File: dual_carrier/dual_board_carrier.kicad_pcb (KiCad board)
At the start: 2 copper layers, 63 x 36.6 mm, 28 parts, among them J1 Conn_01x08, J2 Conn_01x08, J3 Conn_02x10_Top_Bottom, J4 Conn_01x08, J5 Conn_01x08, U1 TJA1051T-3, U2 LM78M05_TO252, U3 TJA1051T-3

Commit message: Add files via upload
Dual Carrier v0.2
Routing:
- net GND: track 79.2 -> 70.7 mm, vias 24 -> 20
- net /CAN_H: track 66.8 -> 62.7 mm
- net +5V: track 101.0 -> 100.4 mm
- added copper zone on F.Cu, net GND
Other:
- board text added: "Dual wideband LSU 4.9 Controller - rusEFI https://rusefi.com/forum/viewtopic.php?f=4&t=1856 https://rusefi.com/forum/viewtopic.php?f=4&t=1927"

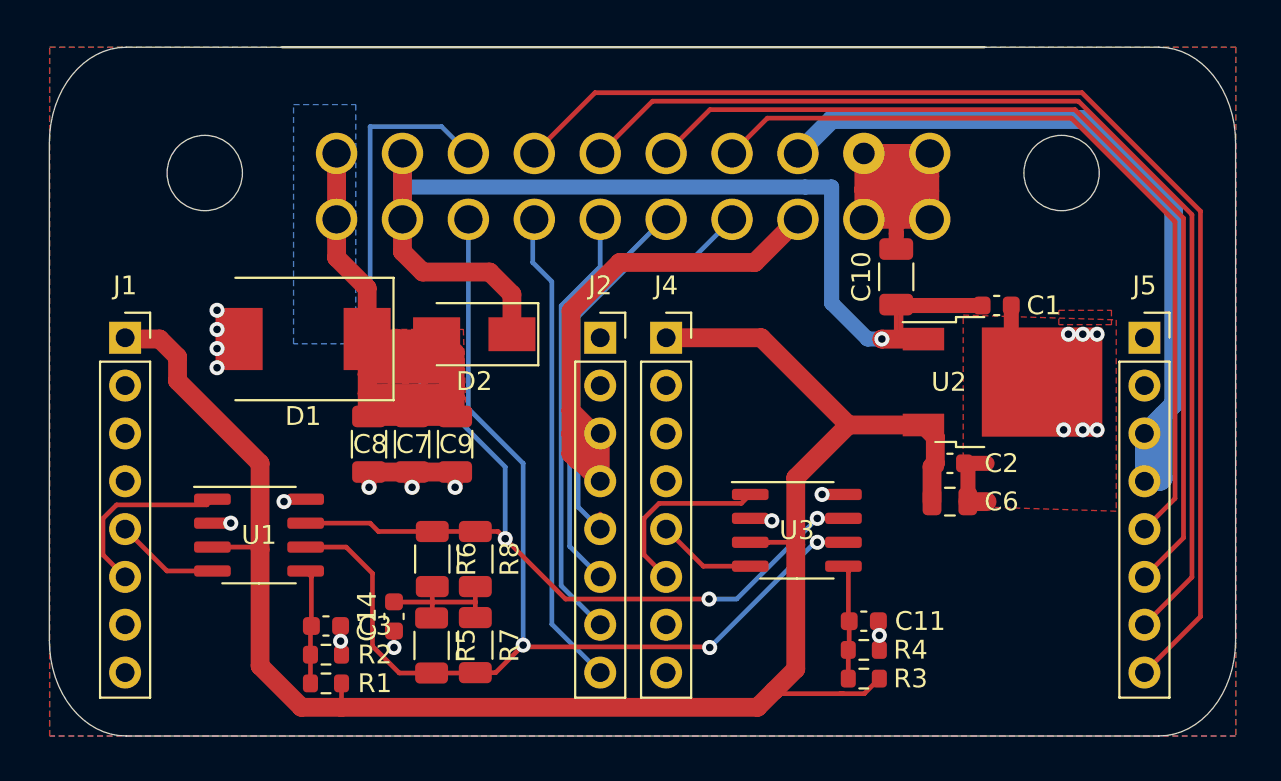
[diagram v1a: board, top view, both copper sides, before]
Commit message: Add files via upload
02/07/21 Updates to dual_carrier and creation of dual_carrier_sxs
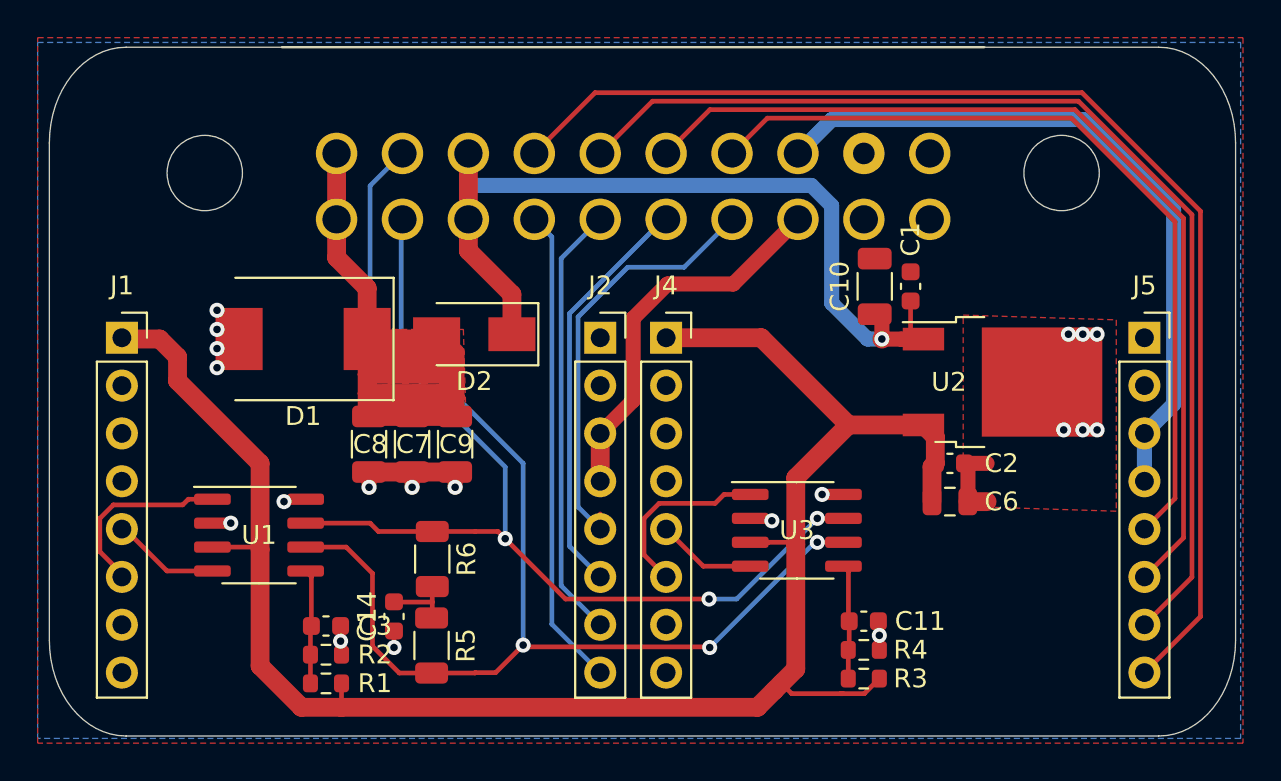
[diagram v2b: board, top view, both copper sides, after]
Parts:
- removed R7, R8: 120, Resistor_SMD:R_1206_3216Metric
- R5, R6: value 120 -> 60
- moved C1 4.68 mm to (144.3, 80.8), turned to 90 degrees
- moved C10 1.25 mm to (142.4, 80.8)
- moved J1 0.17 mm to (102.4, 83.5)
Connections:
- J3 pad 18: /CAN_H -> /LSU_Heater+
- J3 pad 19: /LSU_Heater+ -> /CAN_H
- J3 pad 8: /CAN_L -> /LSU_Heater+
- J3 pad 9: /LSU_Heater+ -> /CAN_L
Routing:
- net GND: track 70.7 -> 26.6 mm
- net /LSU_Heater+: track 63.7 -> 50.2 mm
- net /LSU1_Heater-: track 33.2 -> 20.9 mm
- net /CAN_H: track 62.7 -> 56.1 mm
- net /LSU2_Heater-: track 42.2 -> 37.7 mm
- net Net-(C14-Pad2): track 7.65 -> 3.72 mm
- net /CAN_L: track 60.4 -> 61.9 mm
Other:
- board text added: "CAN H"
- board text added: "CAN L"
- board text added: "Dual wideband LSU 4.9 Controller - rusEFI https://rusefi.com/forum/ viewtopic.php?f=4&t=1856 https://rusefi.com/forum/ viewtopic.php?f=4&t=1927"
- board text added: "Sensor 1"
- board text added: "Sensor 2"
- board text added: "Sensor wiring colors are the same for both connectors. One sensor per row. Use unshielded twisted pair for CAN to ECU."
- board text added: "grey black green"
- board text added: "yellow red white"
- board text removed: "Dual wideband LSU 4.9 Controller - rusEFI https://rusefi.com/forum/viewtopic.php?f=4&t=1856 https://rusefi.com/forum/viewtopic.php?f=4&t=1927"
- board text removed: "black"
- board text removed: "green"
- board text removed: "grey"
- board text removed: "red"
- board text removed: "white"
- board text removed: "yellow"
